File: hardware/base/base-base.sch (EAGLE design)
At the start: 30 parts, among them U1 SD_CARD_SOCKET2041021FFROMTES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, X1 BU-SMA-1-7HOLE

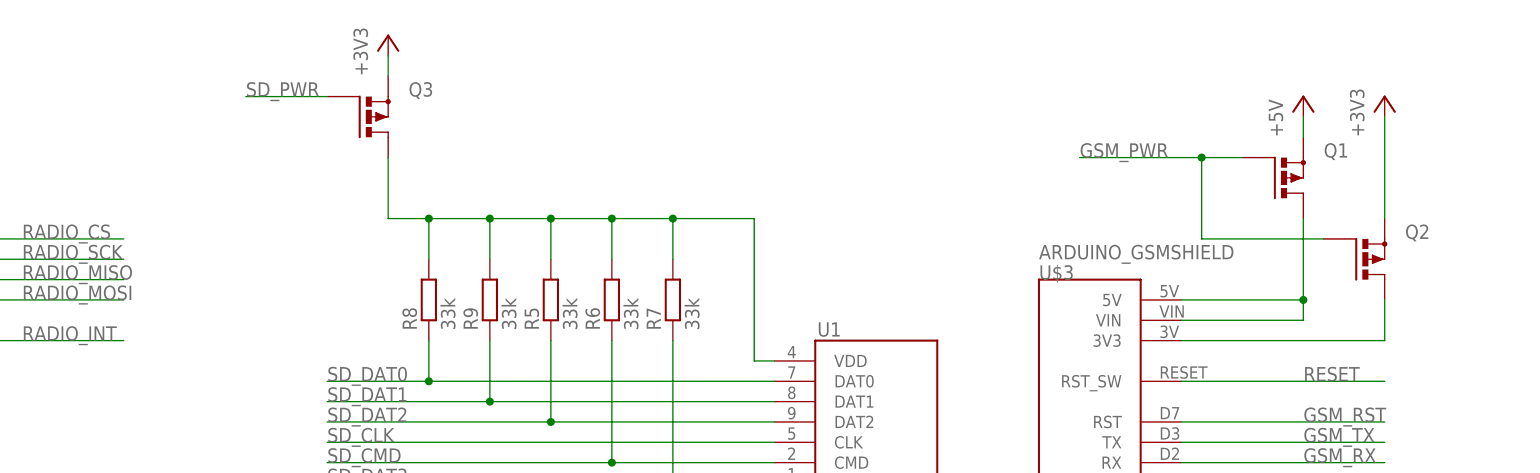
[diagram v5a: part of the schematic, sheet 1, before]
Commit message: BASEHW: Replaced PSU caps with 1206 parts, added transistor to make MOSFETs work with VREG
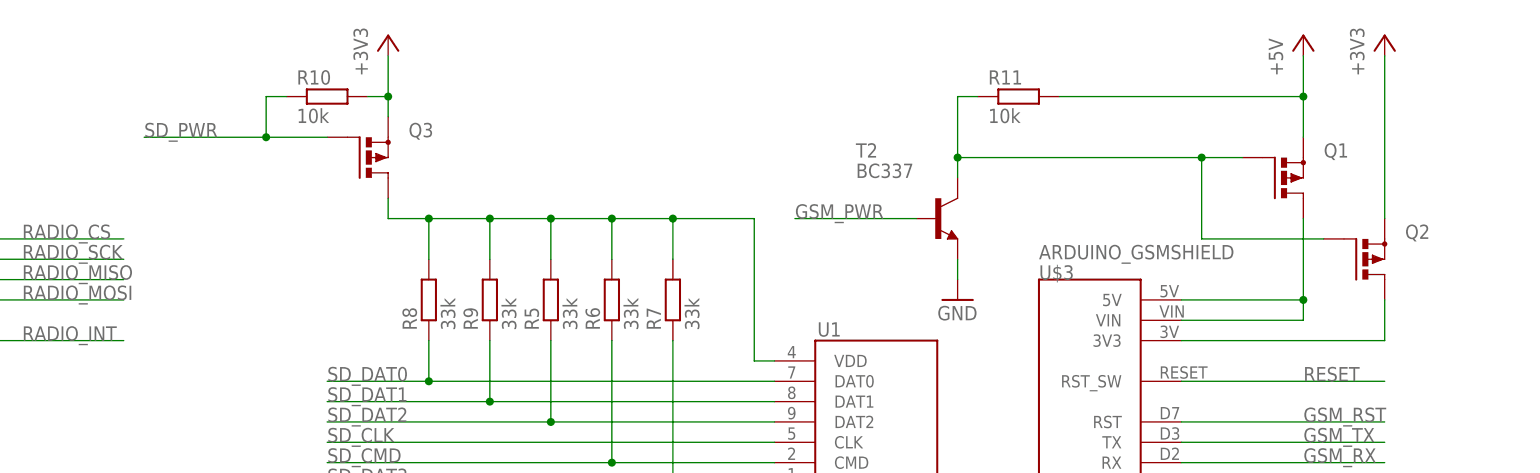
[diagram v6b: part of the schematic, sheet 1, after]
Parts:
- added R10, R11: 10k, resistor:R-EU_0204/7
- added T2: BC337, transistor:BC337
- C1, C3, C4, C6: device SparkFun-Capacitors:CAPPTH -> SparkFun-Capacitors:CAP1206
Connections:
- new net GSM_TRANSISTORLINE: Q1.G, Q2.G, R11.1, T2.C
- net +3V3: now also R10.2
- net +5V: now also R11.2
- net GND: now also T2.E
- net GSM_PWR: now also T2.B, U$1.PD3; no longer Q1.G, Q2.G, U$1.PD4
- net SD_PWR: now also R10.1
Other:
- moved on the sheet: Q3
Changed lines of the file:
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@@
 <part name="U$4" library="FullyCustom" deviceset="TPS563200" device=""/>
 <part name="P+4" library="supply1" deviceset="V+" device=""/>
-<part name="C1" library="SparkFun-Capacitors" deviceset="CAP" device="PTH" value="22u"/>
+<part name="C1" library="SparkFun-Capacitors" deviceset="CAP" device="1206" value="22u"/>
 <part name="C2" library="SparkFun-Capacitors" deviceset="CAP" device="PTH" value="100n"/>
-<part name="C3" library="SparkFun-Capacitors" deviceset="CAP" device="PTH" value="47u"/>
+<part name="C3" library="SparkFun-Capacitors" deviceset="CAP" device="1206" value="47u"/>
 <part name="L1" library="FullyCustom" deviceset="SRR7032" device="" value="2u2"/>
 <part name="R1" library="resistor" deviceset="R-EU_" device="0204/7" value="33k2"/>
@@
 <part name="U$5" library="FullyCustom" deviceset="TPS563200" device=""/>
 <part name="P+5" library="supply1" deviceset="V+" device=""/>
-<part name="C4" library="SparkFun-Capacitors" deviceset="CAP" device="PTH" value="22u"/>
+<part name="C4" library="SparkFun-Capacitors" deviceset="CAP" device="1206" value="22u"/>
 <part name="C5" library="SparkFun-Capacitors" deviceset="CAP" device="PTH" value="100n"/>
-<part name="C6" library="SparkFun-Capacitors" deviceset="CAP" device="PTH" value="47u"/>
+<part name="C6" library="SparkFun-Capacitors" deviceset="CAP" device="1206" value="47u"/>
 <part name="L2" library="FullyCustom" deviceset="SRR7032" device="" value="3u3"/>
 <part name="R3" library="resistor" deviceset="R-EU_" device="0204/7" value="56k2"/>
@@
 <part name="R8" library="resistor" deviceset="R-EU_" device="0204/7" value="33k"/>
 <part name="R9" library="resistor" deviceset="R-EU_" device="0204/7" value="33k"/>
+<part name="R10" library="resistor" deviceset="R-EU_" device="0204/7" value="10k"/>
+<part name="R11" library="resistor" deviceset="R-EU_" device="0204/7" value="10k"/>
+<part name="T2" library="transistor" deviceset="BC337" device=""/>
+<part name="GND11" library="supply1" deviceset="GND" device=""/>
 </parts>
 <sheets>
@@
 <instance part="+3V6" gate="G$1" x="116.84" y="172.72"/>
 <instance part="U$3" gate="G$1" x="205.74" y="139.7"/>
-<instance part="P+3" gate="1" x="231.14" y="165.1"/>
-<instance part="+3V7" gate="G$1" x="241.3" y="165.1"/>
+<instance part="P+3" gate="1" x="231.14" y="172.72"/>
+<instance part="+3V7" gate="G$1" x="241.3" y="172.72"/>
 <instance part="GND7" gate="1" x="231.14" y="106.68"/>
 <instance part="Q1" gate="G$1" x="228.6" y="154.94"/>
 <instance part="Q2" gate="G$1" x="238.76" y="144.78"/>
-<instance part="Q3" gate="G$1" x="114.3" y="162.56"/>
+<instance part="Q3" gate="G$1" x="114.3" y="157.48"/>
 <instance part="U$4" gate="1" x="58.42" y="68.58"/>
 <instance part="P+4" gate="1" x="48.26" y="81.28"/>
@@
 <instance part="R8" gate="G$1" x="121.92" y="139.7" rot="R90"/>
 <instance part="R9" gate="G$1" x="129.54" y="139.7" rot="R90"/>
+<instance part="R10" gate="G$1" x="109.22" y="165.1"/>
+<instance part="R11" gate="G$1" x="195.58" y="165.1"/>
+<instance part="T2" gate="G$1" x="185.42" y="149.86"/>
+<instance part="GND11" gate="1" x="187.96" y="139.7"/>
 </instances>
 <busses>
@@
 <pinref part="Q2" gate="G$1" pin="S"/>
 <pinref part="+3V7" gate="G$1" pin="+3V3"/>
-<wire x1="241.3" y1="149.86" x2="241.3" y2="162.56" width="0.1524" layer="91"/>
+<wire x1="241.3" y1="149.86" x2="241.3" y2="170.18" width="0.1524" layer="91"/>
 </segment>
 <segment>
 <pinref part="Q3" gate="G$1" pin="S"/>
 <pinref part="+3V6" gate="G$1" pin="+3V3"/>
-<wire x1="116.84" y1="167.64" x2="116.84" y2="170.18" width="0.1524" layer="91"/>
+<wire x1="116.84" y1="162.56" x2="116.84" y2="165.1" width="0.1524" layer="91"/>
+<pinref part="R10" gate="G$1" pin="2"/>
+<wire x1="116.84" y1="165.1" x2="116.84" y2="170.18" width="0.1524" layer="91"/>
+<wire x1="114.3" y1="165.1" x2="116.84" y2="165.1" width="0.1524" layer="91"/>
+<junction x="116.84" y="165.1"/>
 </segment>
 <segment>
@@
 <wire x1="60.96" y1="109.22" x2="86.36" y2="109.22" width="0.1524" layer="91"/>
 </segment>
+<segment>
+<pinref part="GND11" gate="1" pin="GND"/>
+<pinref part="T2" gate="G$1" pin="E"/>
+<wire x1="187.96" y1="142.24" x2="187.96" y2="144.78" width="0.1524" layer="91"/>
+</segment>
 </net>
 <net name="RADIO_CS" class="0">
@@
 <pinref part="P+3" gate="1" pin="+5V"/>
 <pinref part="Q1" gate="G$1" pin="S"/>
-<wire x1="231.14" y1="162.56" x2="231.14" y2="160.02" width="0.1524" layer="91"/>
+<wire x1="231.14" y1="170.18" x2="231.14" y2="165.1" width="0.1524" layer="91"/>
+<pinref part="R11" gate="G$1" pin="2"/>
+<wire x1="231.14" y1="165.1" x2="231.14" y2="160.02" width="0.1524" layer="91"/>
+<wire x1="200.66" y1="165.1" x2="231.14" y2="165.1" width="0.1524" layer="91"/>
+<junction x="231.14" y="165.1"/>
 </segment>
 <segment>
@@
 <net name="GSM_PWR" class="0">
 <segment>
-<pinref part="Q2" gate="G$1" pin="G"/>
-<wire x1="233.68" y1="147.32" x2="218.44" y2="147.32" width="0.1524" layer="91"/>
-<wire x1="218.44" y1="147.32" x2="218.44" y2="157.48" width="0.1524" layer="91"/>
-<pinref part="Q1" gate="G$1" pin="G"/>
-<wire x1="218.44" y1="157.48" x2="223.52" y2="157.48" width="0.1524" layer="91"/>
-<wire x1="218.44" y1="157.48" x2="203.2" y2="157.48" width="0.1524" layer="91"/>
-<junction x="218.44" y="157.48"/>
-<label x="203.2" y="157.48" size="1.778" layer="95"/>
-</segment>
-<segment>
 <pinref part="U$5" gate="1" pin="EN"/>
 <wire x1="180.34" y1="63.5" x2="147.32" y2="63.5" width="0.1524" layer="91"/>
 <label x="147.32" y="63.5" size="1.778" layer="95"/>
 </segment>
+<segment>
+<pinref part="T2" gate="G$1" pin="B"/>
+<wire x1="182.88" y1="149.86" x2="167.64" y2="149.86" width="0.1524" layer="91"/>
+<label x="167.64" y="149.86" size="1.778" layer="95"/>
+</segment>
 </net>
 <net name="SD_PWR" class="0">
 <segment>
 <pinref part="Q3" gate="G$1" pin="G"/>
-<wire x1="109.22" y1="165.1" x2="99.06" y2="165.1" width="0.1524" layer="91"/>
-<label x="99.06" y="165.1" size="1.778" layer="95"/>
+<wire x1="109.22" y1="160.02" x2="101.6" y2="160.02" width="0.1524" layer="91"/>
+<label x="86.36" y="160.02" size="1.778" layer="95"/>
+<pinref part="R10" gate="G$1" pin="1"/>
+<wire x1="101.6" y1="160.02" x2="86.36" y2="160.02" width="0.1524" layer="91"/>
+<wire x1="104.14" y1="165.1" x2="101.6" y2="165.1" width="0.1524" layer="91"/>
+<wire x1="101.6" y1="165.1" x2="101.6" y2="160.02" width="0.1524" layer="91"/>
+<junction x="101.6" y="160.02"/>
 </segment>
 </net>
@@
 <pinref part="R8" gate="G$1" pin="2"/>
 <pinref part="Q3" gate="G$1" pin="D"/>
-<wire x1="116.84" y1="157.48" x2="116.84" y2="149.86" width="0.1524" layer="91"/>
+<wire x1="116.84" y1="152.4" x2="116.84" y2="149.86" width="0.1524" layer="91"/>
 <wire x1="116.84" y1="149.86" x2="121.92" y2="149.86" width="0.1524" layer="91"/>
 <wire x1="121.92" y1="149.86" x2="129.54" y2="149.86" width="0.1524" layer="91"/>
@@
 <wire x1="121.92" y1="144.78" x2="121.92" y2="149.86" width="0.1524" layer="91"/>
 <junction x="121.92" y="149.86"/>
+</segment>
+</net>
+<net name="GSM_TRANSISTORLINE" class="0">
+<segment>
+<pinref part="Q2" gate="G$1" pin="G"/>
+<wire x1="233.68" y1="147.32" x2="218.44" y2="147.32" width="0.1524" layer="91"/>
+<wire x1="218.44" y1="147.32" x2="218.44" y2="157.48" width="0.1524" layer="91"/>
+<pinref part="Q1" gate="G$1" pin="G"/>
+<wire x1="218.44" y1="157.48" x2="223.52" y2="157.48" width="0.1524" layer="91"/>
+<pinref part="R11" gate="G$1" pin="1"/>
+<wire x1="190.5" y1="165.1" x2="187.96" y2="165.1" width="0.1524" layer="91"/>
+<pinref part="T2" gate="G$1" pin="C"/>
+<wire x1="187.96" y1="165.1" x2="187.96" y2="157.48" width="0.1524" layer="91"/>
+<wire x1="187.96" y1="157.48" x2="187.96" y2="154.94" width="0.1524" layer="91"/>
+<wire x1="218.44" y1="157.48" x2="187.96" y2="157.48" width="0.1524" layer="91"/>
+<junction x="218.44" y="157.48"/>
+<junction x="187.96" y="157.48"/>
 </segment>
 </net>
@@
 </segment>
 </net>
-<net name="GSM_PWR" class="0">
-<segment>
-<pinref part="U$1" gate="G$1" pin="PD4"/>
-<wire x1="182.88" y1="91.44" x2="203.2" y2="91.44" width="0.1524" layer="91"/>
-<label x="190.5" y="91.44" size="1.778" layer="95"/>
-</segment>
-</net>
 <net name="SD_PWR" class="0">
 <segment>
@@
 </segment>
 </net>
+<net name="GSM_PWR" class="0">
+<segment>
+<pinref part="U$1" gate="G$1" pin="PD3"/>
+<wire x1="152.4" y1="91.44" x2="132.08" y2="91.44" width="0.1524" layer="91"/>
+<label x="132.08" y="91.44" size="1.778" layer="95"/>
+</segment>
+</net>

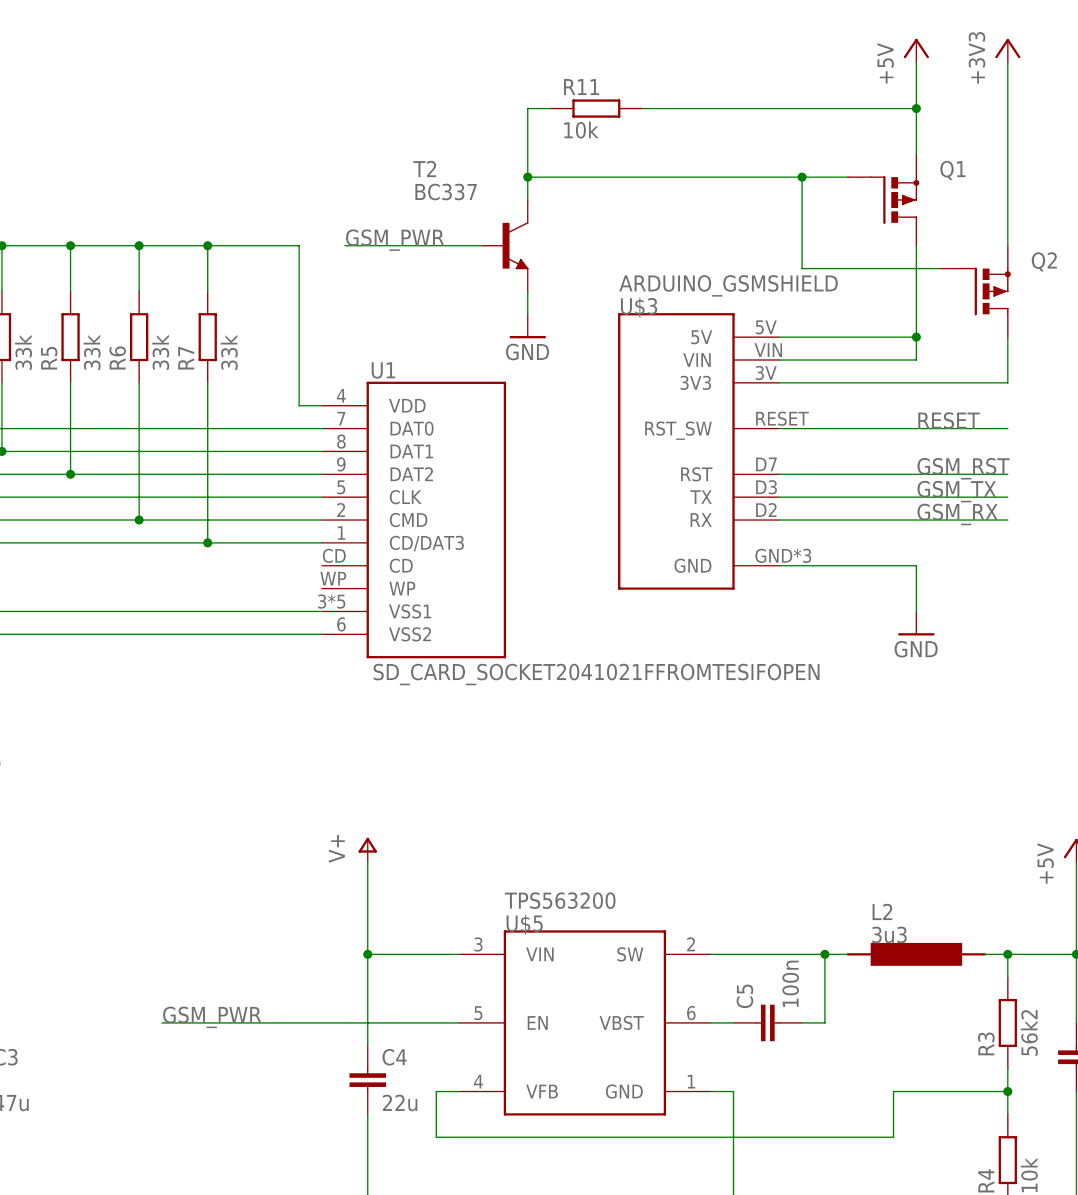
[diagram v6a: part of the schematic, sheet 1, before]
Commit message: Fixed bad transistor setup
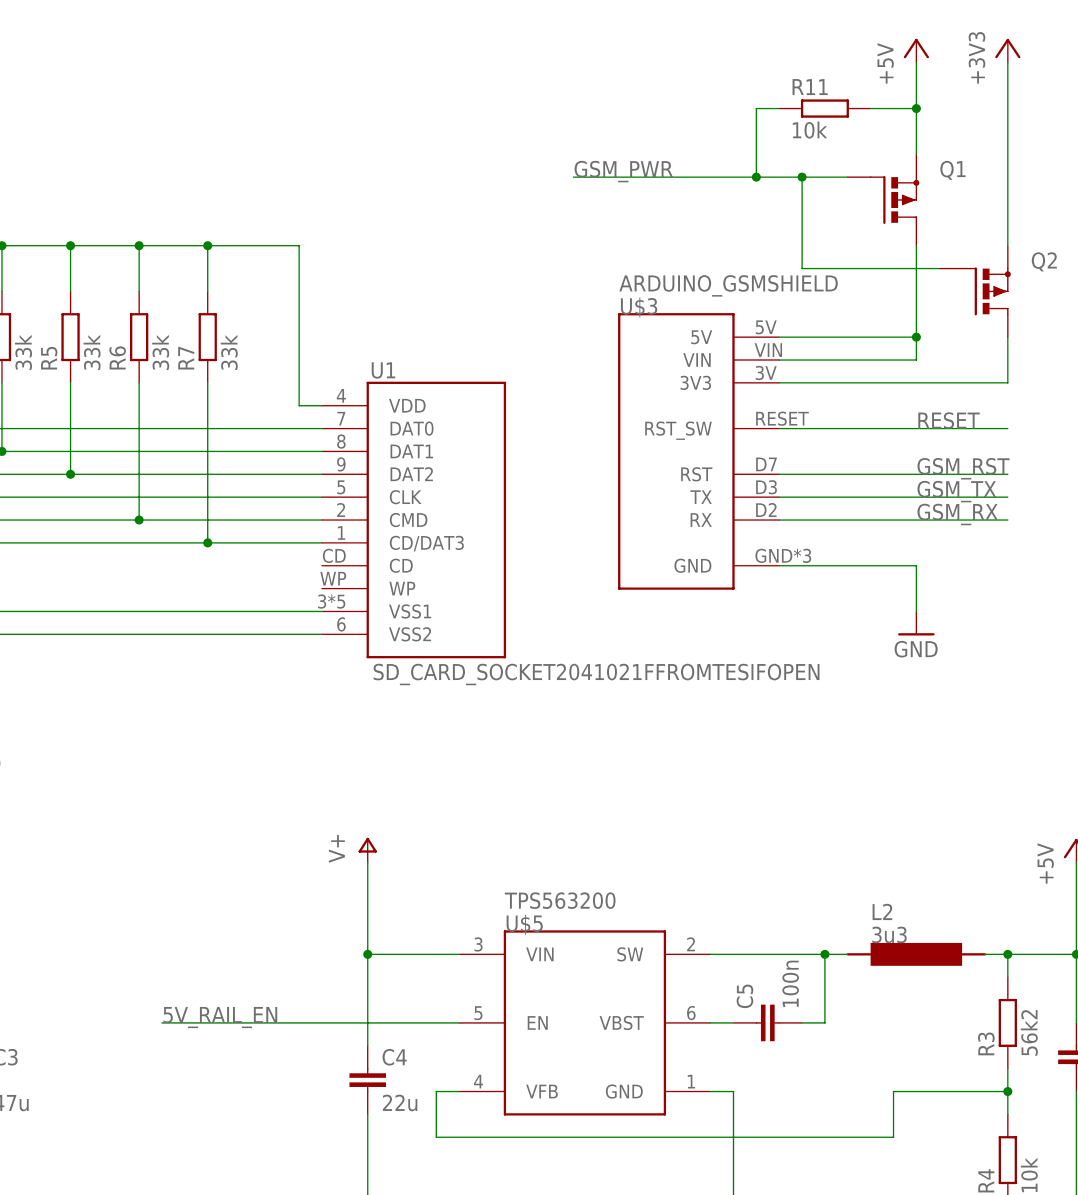
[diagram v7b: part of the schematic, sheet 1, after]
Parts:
- removed T2: BC337, transistor:BC337
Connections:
- removed net GSM_TRANSISTORLINE: Q1.G, Q2.G, R11.1, T2.C
- new net 5V_RAIL_EN: U$1.PD9, U$5.EN
- net GND: no longer T2.E
- net GSM_PWR: now also Q1.G, Q2.G, R11.1; no longer T2.B, U$5.EN
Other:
- moved on the sheet: R11
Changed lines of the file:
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@@
 <part name="R10" library="resistor" deviceset="R-EU_" device="0204/7" value="10k"/>
 <part name="R11" library="resistor" deviceset="R-EU_" device="0204/7" value="10k"/>
-<part name="T2" library="transistor" deviceset="BC337" device=""/>
-<part name="GND11" library="supply1" deviceset="GND" device=""/>
 </parts>
 <sheets>
@@
 <instance part="R9" gate="G$1" x="129.54" y="139.7" rot="R90"/>
 <instance part="R10" gate="G$1" x="109.22" y="165.1"/>
-<instance part="R11" gate="G$1" x="195.58" y="165.1"/>
-<instance part="T2" gate="G$1" x="185.42" y="149.86"/>
-<instance part="GND11" gate="1" x="187.96" y="139.7"/>
+<instance part="R11" gate="G$1" x="220.98" y="165.1"/>
 </instances>
 <busses>
@@
 <wire x1="60.96" y1="109.22" x2="86.36" y2="109.22" width="0.1524" layer="91"/>
 </segment>
-<segment>
-<pinref part="GND11" gate="1" pin="GND"/>
-<pinref part="T2" gate="G$1" pin="E"/>
-<wire x1="187.96" y1="142.24" x2="187.96" y2="144.78" width="0.1524" layer="91"/>
-</segment>
 </net>
 <net name="RADIO_CS" class="0">
@@
 <pinref part="R11" gate="G$1" pin="2"/>
 <wire x1="231.14" y1="165.1" x2="231.14" y2="160.02" width="0.1524" layer="91"/>
-<wire x1="200.66" y1="165.1" x2="231.14" y2="165.1" width="0.1524" layer="91"/>
+<wire x1="226.06" y1="165.1" x2="231.14" y2="165.1" width="0.1524" layer="91"/>
 <junction x="231.14" y="165.1"/>
 </segment>
@@
 <net name="GSM_PWR" class="0">
 <segment>
-<pinref part="U$5" gate="1" pin="EN"/>
-<wire x1="180.34" y1="63.5" x2="147.32" y2="63.5" width="0.1524" layer="91"/>
-<label x="147.32" y="63.5" size="1.778" layer="95"/>
-</segment>
-<segment>
-<pinref part="T2" gate="G$1" pin="B"/>
-<wire x1="182.88" y1="149.86" x2="167.64" y2="149.86" width="0.1524" layer="91"/>
-<label x="167.64" y="149.86" size="1.778" layer="95"/>
+<pinref part="Q2" gate="G$1" pin="G"/>
+<wire x1="233.68" y1="147.32" x2="218.44" y2="147.32" width="0.1524" layer="91"/>
+<wire x1="218.44" y1="147.32" x2="218.44" y2="157.48" width="0.1524" layer="91"/>
+<pinref part="Q1" gate="G$1" pin="G"/>
+<wire x1="218.44" y1="157.48" x2="223.52" y2="157.48" width="0.1524" layer="91"/>
+<wire x1="218.44" y1="157.48" x2="213.36" y2="157.48" width="0.1524" layer="91"/>
+<junction x="218.44" y="157.48"/>
+<label x="193.04" y="157.48" size="1.778" layer="95"/>
+<pinref part="R11" gate="G$1" pin="1"/>
+<wire x1="213.36" y1="157.48" x2="193.04" y2="157.48" width="0.1524" layer="91"/>
+<wire x1="215.9" y1="165.1" x2="213.36" y2="165.1" width="0.1524" layer="91"/>
+<wire x1="213.36" y1="165.1" x2="213.36" y2="157.48" width="0.1524" layer="91"/>
+<junction x="213.36" y="157.48"/>
 </segment>
 </net>
@@
 </segment>
 </net>
-<net name="GSM_TRANSISTORLINE" class="0">
-<segment>
-<pinref part="Q2" gate="G$1" pin="G"/>
-<wire x1="233.68" y1="147.32" x2="218.44" y2="147.32" width="0.1524" layer="91"/>
-<wire x1="218.44" y1="147.32" x2="218.44" y2="157.48" width="0.1524" layer="91"/>
-<pinref part="Q1" gate="G$1" pin="G"/>
-<wire x1="218.44" y1="157.48" x2="223.52" y2="157.48" width="0.1524" layer="91"/>
-<pinref part="R11" gate="G$1" pin="1"/>
-<wire x1="190.5" y1="165.1" x2="187.96" y2="165.1" width="0.1524" layer="91"/>
-<pinref part="T2" gate="G$1" pin="C"/>
-<wire x1="187.96" y1="165.1" x2="187.96" y2="157.48" width="0.1524" layer="91"/>
-<wire x1="187.96" y1="157.48" x2="187.96" y2="154.94" width="0.1524" layer="91"/>
-<wire x1="218.44" y1="157.48" x2="187.96" y2="157.48" width="0.1524" layer="91"/>
-<junction x="218.44" y="157.48"/>
-<junction x="187.96" y="157.48"/>
+<net name="5V_RAIL_EN" class="0">
+<segment>
+<pinref part="U$5" gate="1" pin="EN"/>
+<wire x1="180.34" y1="63.5" x2="147.32" y2="63.5" width="0.1524" layer="91"/>
+<label x="147.32" y="63.5" size="1.778" layer="95"/>
 </segment>
 </net>
@@
 </segment>
 </net>
+<net name="5V_RAIL_EN" class="0">
+<segment>
+<pinref part="U$1" gate="G$1" pin="PD9"/>
+<wire x1="66.04" y1="78.74" x2="43.18" y2="78.74" width="0.1524" layer="91"/>
+<label x="43.18" y="78.74" size="1.778" layer="95"/>
+</segment>
+</net>
